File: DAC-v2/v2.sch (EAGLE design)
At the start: 16 parts, among them Q1 IRF520, Q2 IRF520, Q3 IRF520

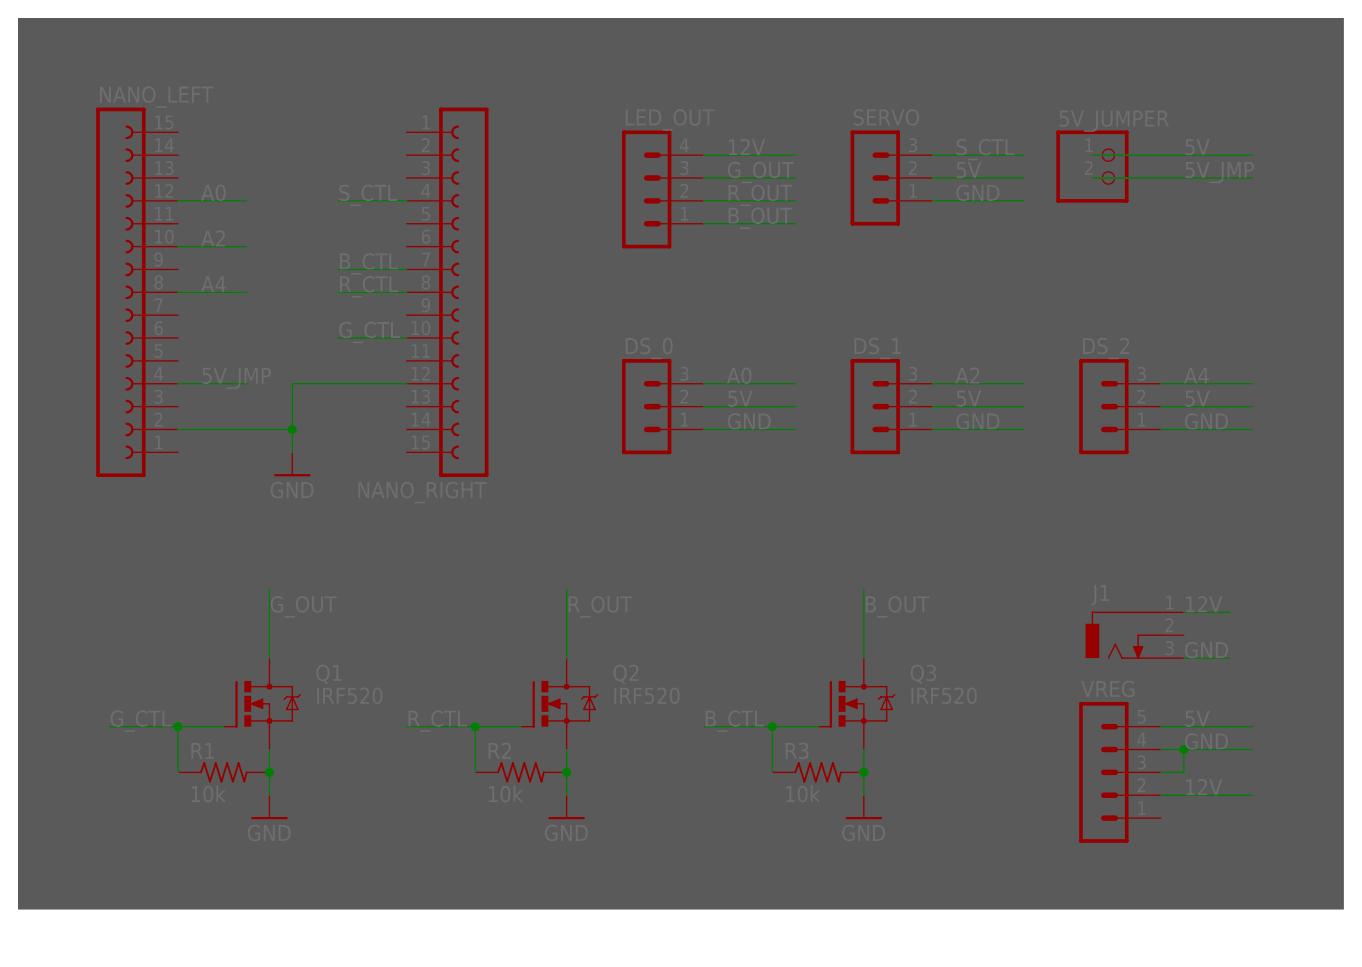
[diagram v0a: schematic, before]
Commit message: Updated casemod circuit, added a few images
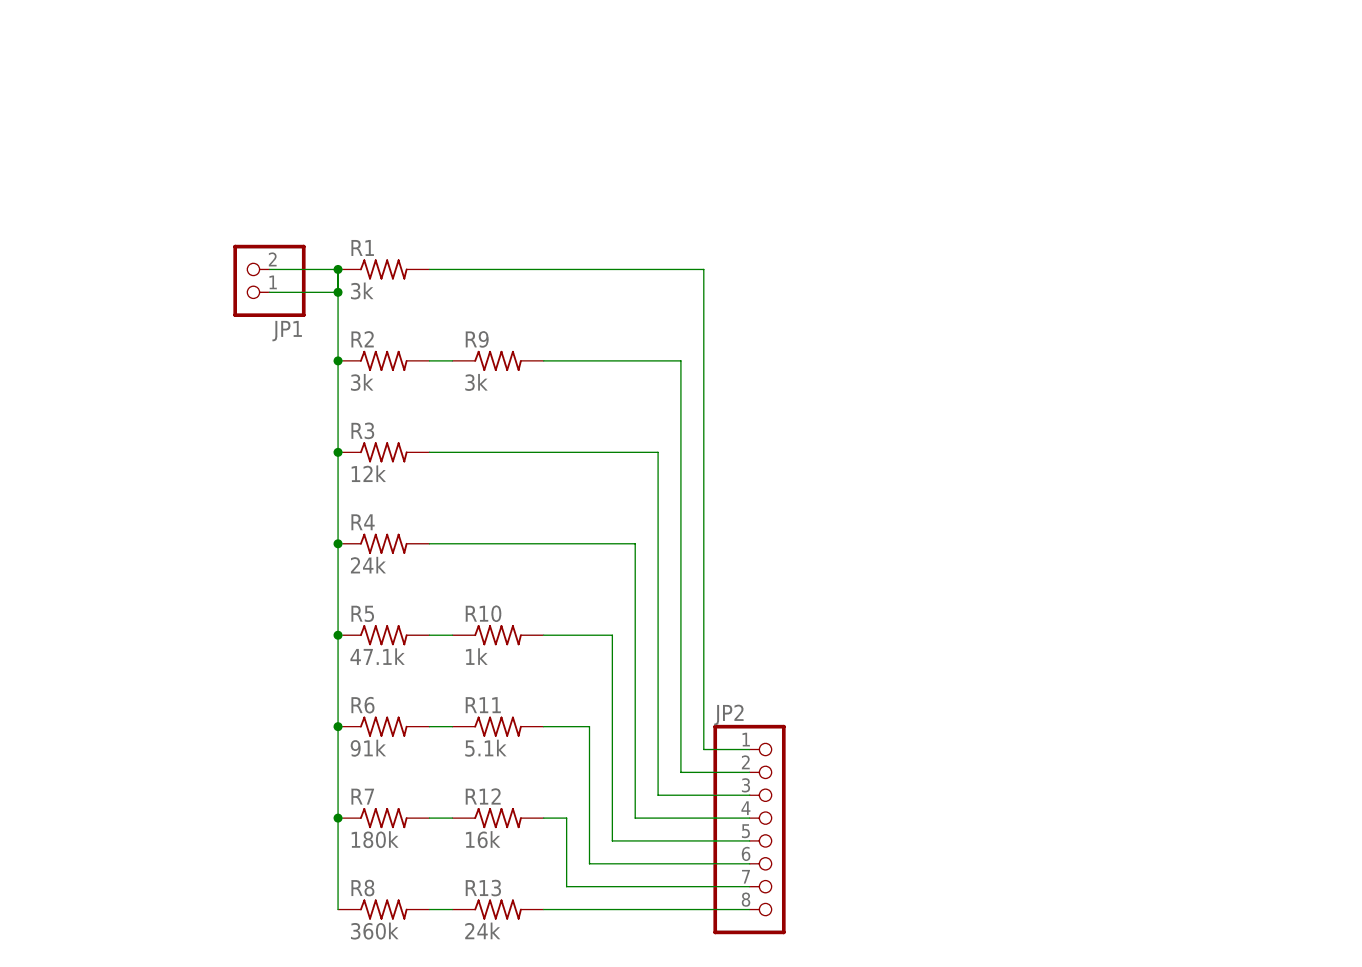
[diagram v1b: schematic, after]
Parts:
- removed 5V_JUMPER: (no value), pinhead:PINHD-1X2
- removed DS_0, DS_1, DS_2, SERVO: (no value), con-lstb:MA03-1
- removed J1: (no value), con-jack:DCJ0303
- removed LED_OUT: (no value), con-lstb:MA04-1
- removed NANO_LEFT, NANO_RIGHT: (no value), con-lsta:FE15-1
- removed Q1, Q2, Q3: IRF520, transistor-power:IRF520
- removed VREG: (no value), con-lstb:MA05-1
- added JP1: (no value), pinhead:PINHD-1X2
- added JP2: (no value), pinhead:PINHD-1X8
- added R10: 1k, rcl:R-US_0309/10
- added R11: 5.1k, rcl:R-US_0309/10
- added R12: 16k, rcl:R-US_0309/10
- added R13, R4: 24k, rcl:R-US_0309/10
- added R5: 47.1k, rcl:R-US_0309/10
- added R6: 91k, rcl:R-US_0309/10
- added R7: 180k, rcl:R-US_0309/10
- added R8: 360k, rcl:R-US_0309/10
- added R9: 3k, rcl:R-US_0309/10
- R1, R2: value 10k -> 3k; device rcl:R-US_0207/7 -> rcl:R-US_0309/10
- R3: value 10k -> 12k; device rcl:R-US_0207/7 -> rcl:R-US_0309/10
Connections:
- removed net 12V: J1.1, LED_OUT.4, VREG.2
- removed net 5V: 5V_JUMPER.1, DS_0.2, DS_1.2, DS_2.2, SERVO.2, VREG.5
- removed net 5V_JMP: 5V_JUMPER.2, NANO_LEFT.4
- removed net A0: DS_0.3, NANO_LEFT.12
- removed net A2: DS_1.3, NANO_LEFT.10
- removed net A4: DS_2.3, NANO_LEFT.8
- removed net B_CTL: NANO_RIGHT.7, Q3.G, R3.1
- removed net B_OUT: LED_OUT.1, Q3.D
- removed net GND: DS_0.1, DS_1.1, DS_2.1, J1.3, NANO_LEFT.2, NANO_RIGHT.12, Q1.S, Q2.S, Q3.S, R1.2, R2.2, R3.2, SERVO.1, VREG.3, VREG.4
- removed net G_CTL: NANO_RIGHT.10, Q1.G, R1.1
- removed net G_OUT: LED_OUT.3, Q1.D
- removed net R_CTL: NANO_RIGHT.8, Q2.G, R2.1
- removed net R_OUT: LED_OUT.2, Q2.D
- removed net S_CTL: NANO_RIGHT.4, SERVO.3
- new net N$1: JP1.1, JP1.2, R1.1, R2.1, R3.1, R4.1, R5.1, R6.1, R7.1, R8.1
- new net N$10: JP2.3, R3.2
- new net N$11: JP2.4, R4.2
- new net N$12: JP2.5, R10.2
- new net N$13: JP2.6, R11.2
- new net N$14: JP2.7, R12.2
- new net N$2: R12.1, R7.2
- new net N$3: R13.1, R8.2
- new net N$4: JP2.8, R13.2
- new net N$5: R2.2, R9.1
- new net N$6: R10.1, R5.2
- new net N$7: R11.1, R6.2
- new net N$8: JP2.1, R1.2
- new net N$9: JP2.2, R9.2
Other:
- note removed: "Arduino Connections"
- note removed: "Input/Output"
- note removed: "LED Controller"
- note removed: "Power"
- moved on the sheet: R1, R2, R3
